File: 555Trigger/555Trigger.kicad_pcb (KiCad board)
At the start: 2 copper layers, 39 parts, among them J1 Conn_01x03_Socket, J2 Conn_01x02_Socket, J3 Strobing_LED_1, J4 Strobing_LED_2, U7 74LVC2G74, U8 74AHC2G00, U9 OPA2333xxD

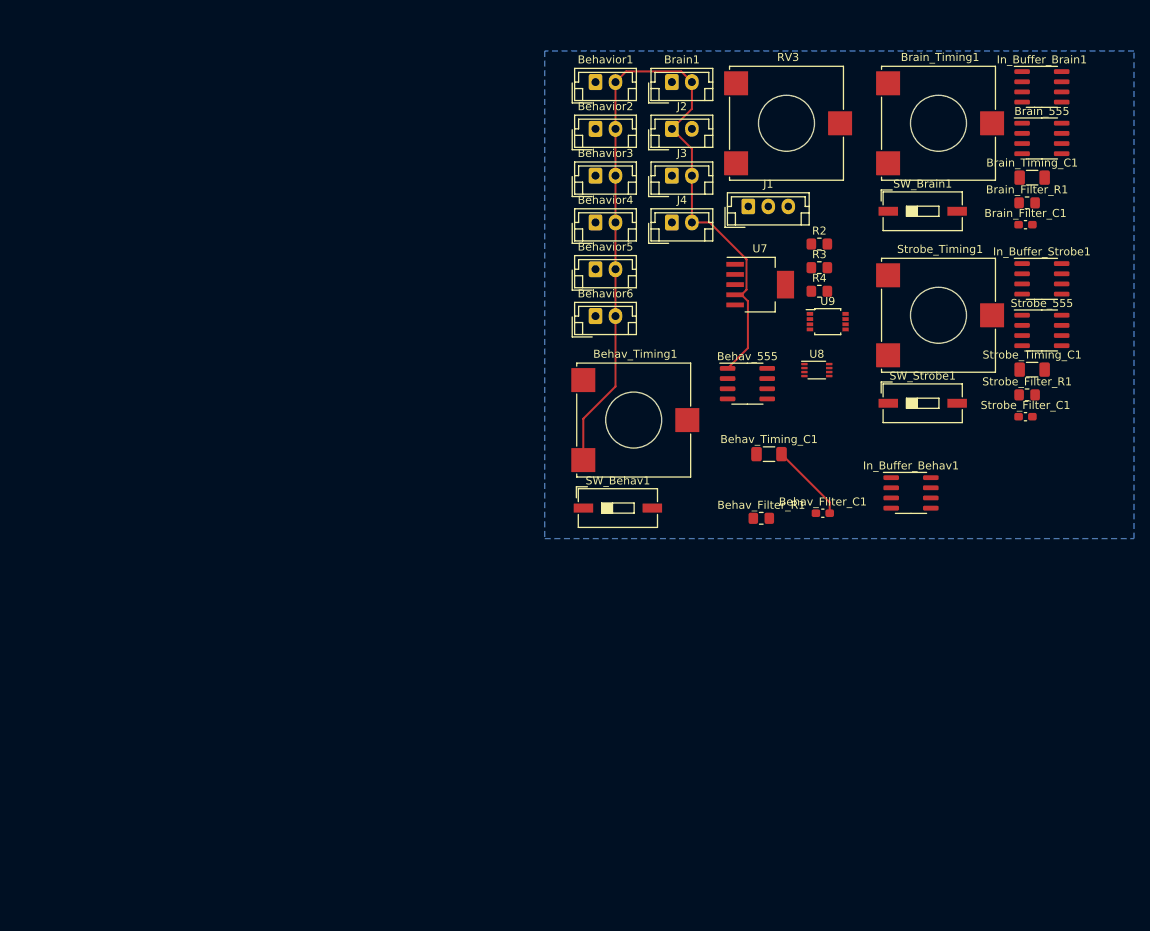
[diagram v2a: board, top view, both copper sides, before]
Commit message: updated timer design
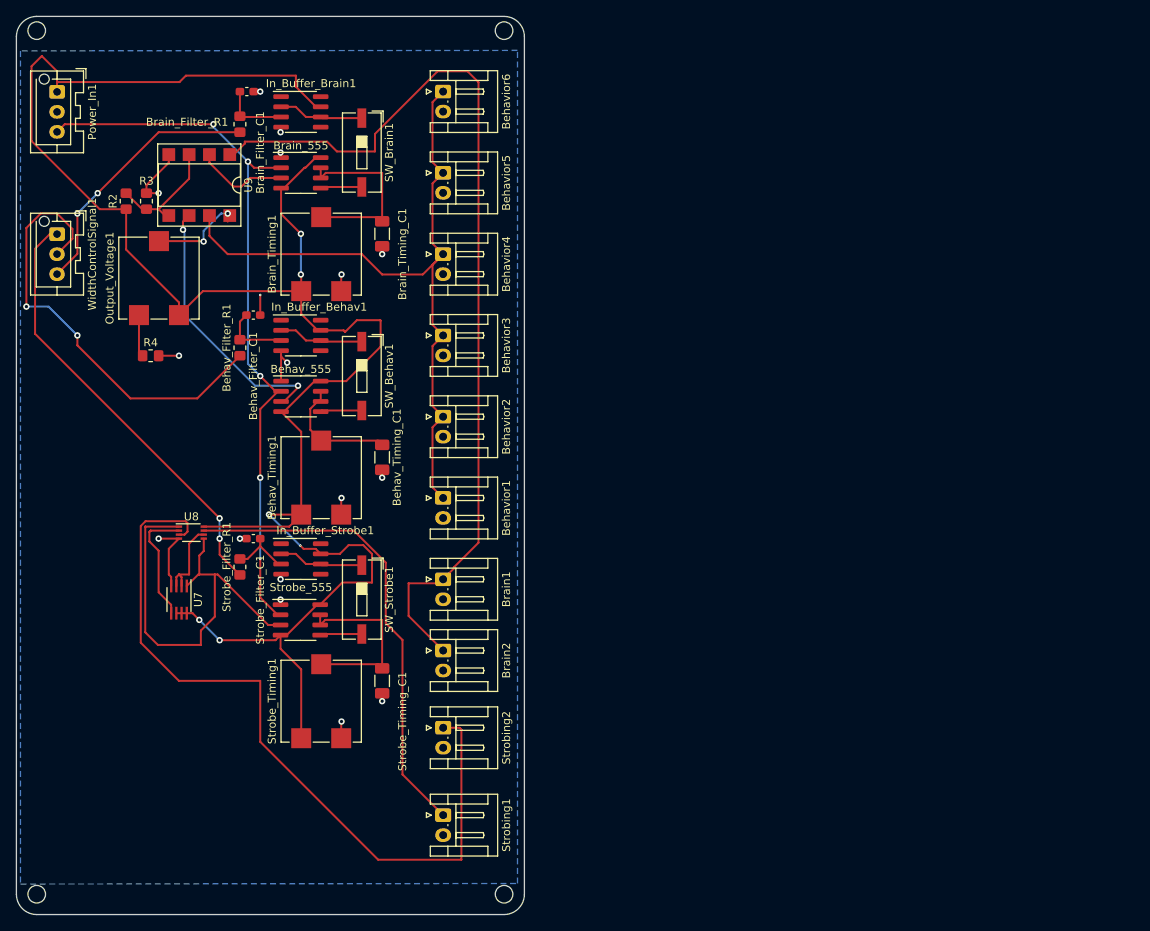
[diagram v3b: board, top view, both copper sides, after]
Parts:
- removed J2: Conn_01x02_Socket, Connector_JST:JST_EH_B2B-EH-A_1x02_P2.50mm_Vertical
- added Brain2: Conn_01x02_Socket, Connector_JST:JST_EH_S2B-EH_1x02_P2.50mm_Horizontal, F.Cu at (78.7, 100.3)
- added H1: MountingHole, MountingHole:MountingHole_2.2mm_M2, F.Cu at (86.4, 22.9)
- added H2: MountingHole, MountingHole:MountingHole_2.2mm_M2, F.Cu at (27.9, 22.9)
- added H3: MountingHole, MountingHole:MountingHole_2.2mm_M2, F.Cu at (27.9, 130.8)
- added H4: MountingHole, MountingHole:MountingHole_2.2mm_M2, F.Cu at (86.4, 130.8)
- added Power_In1: Conn_01x03_Socket, Connector_JST:JST_XA_B03B-XASK-1-A_1x03_P2.50mm_Vertical, F.Cu at (30.5, 30.5)
- Behav_555, Brain_555, Strobe_555: value ~ -> TLC555xD
- Behav_Timing1, Brain_Timing1, Strobe_Timing1: footprint Potentiometer_SMD:Potentiometer_ACP_CA14-VSMD_Vertical_Hole -> Potentiometer_SMD:Potentiometer_ACP_CA9-VSMD_Vertical
- Behavior1, Behavior2, Behavior3, Behavior4, Behavior5, Behavior6, Brain1: footprint Connector_JST:JST_EH_B2B-EH-A_1x02_P2.50mm_Vertical -> Connector_JST:JST_EH_S2B-EH_1x02_P2.50mm_Horizontal
- Output_Voltage1: renamed from RV3; footprint Potentiometer_SMD:Potentiometer_ACP_CA14-VSMD_Vertical_Hole -> Potentiometer_SMD:Potentiometer_ACP_CA9-VSMD_Vertical
- Strobing1: renamed from J3; value Strobing_LED_1 -> Conn_01x02_Socket; footprint Connector_JST:JST_EH_B2B-EH-A_1x02_P2.50mm_Vertical -> Connector_JST:JST_EH_S2B-EH_1x02_P2.50mm_Horizontal
- Strobing2: renamed from J4; value Strobing_LED_2 -> Conn_01x02_Socket; footprint Connector_JST:JST_EH_B2B-EH-A_1x02_P2.50mm_Vertical -> Connector_JST:JST_EH_S2B-EH_1x02_P2.50mm_Horizontal
- U7: footprint Package_TO_SOT_SMD:SOT-223-6_TabPin3 -> Package_SO:SSOP-8_2.95x2.8mm_P0.65mm
- U9: footprint Package_SO:OnSemi_Micro8 -> Package_DIP:DIP-8_W7.62mm_SMDSocket_SmallPads
- WidthControlSignal1: renamed from J1; footprint Connector_JST:JST_EH_B3B-EH-A_1x03_P2.50mm_Vertical -> Connector_JST:JST_XA_B03B-XASK-1-A_1x03_P2.50mm_Vertical
- moved Strobe_Filter_R1 100.7 mm to (53.3, 89.9), turned to 90 degrees
- moved Strobe_555 99.5 mm to (60.9, 96.5)
- moved In_Buffer_Strobe1 99.0 mm to (61.0, 88.9)
- moved Brain_Filter_R1 98.9 mm to (53.3, 34.6), turned to 90 degrees
- moved Brain_Filter_C1 98.7 mm to (54.2, 30.5)
- moved Strobe_Filter_C1 97.7 mm to (55.0, 86.4), turned to 180 degrees
- moved Brain_555 92.7 mm to (61.0, 40.6)
- moved In_Buffer_Brain1 92.7 mm to (61.0, 33.0)
- moved Strobe_Timing1 91.2 mm to (63.5, 106.7), turned to 90 degrees
- moved Strobe_Timing_C1 90.1 mm to (71.1, 104.1), turned to -90 degrees
- moved R2 86.8 mm to (39.1, 44.2), turned to 90 degrees
- moved WidthControlSignal1 86.5 mm to (30.5, 48.3), turned to -90 degrees
- moved Strobing1 84.9 mm to (78.7, 120.9), turned to -90 degrees
- moved R3 84.5 mm to (41.7, 44.2), turned to 90 degrees
- moved R4 84.0 mm to (42.2, 63.5)
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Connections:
- net /Behavior_Camera_Unit/Trigger_In renamed VAC
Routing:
- net +5V: track 0.00 -> 246.8 mm, vias 0 -> 6
- net Net-(Brain1-Pin_1): track 0.00 -> 117.0 mm
- net Net-(Strobing2-Pin_1): track 0.00 -> 97.5 mm
- net VAC: track 0.00 -> 92.2 mm, vias 0 -> 5
- net Net-(Behavior1-Pin_1): track 0.00 -> 91.1 mm
- net GND: track 113.9 -> 40.1 mm, vias 0 -> 17
- net Net-(Strobing1-Pin_1): track 0.00 -> 58.9 mm
- net /Behavior_Camera_Unit/CV_In: track 0.00 -> 55.5 mm, vias 0 -> 2
- net /Strobing_Trigger/CV_In: track 0.00 -> 54.9 mm, vias 0 -> 2
- net /Strobing_Trigger/Trigger_Out: track 0.00 -> 54.2 mm
- net /Behavior_Camera_Unit/Trigger_Out: track 0.00 -> 34.2 mm, vias 0 -> 2
- net /Brain_Camera_Unit/CV_In: track 0.00 -> 33.2 mm, vias 0 -> 2
- net Net-(Strobe_555-DIS): track 0.00 -> 23.2 mm
- net Net-(Brain_555-DIS): track 0.00 -> 23.1 mm
- net Net-(Behav_555-DIS): track 0.00 -> 15.3 mm
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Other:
- board outline added: 63.5 x 112.3 mm

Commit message: changed some components to make manufacturing simpler
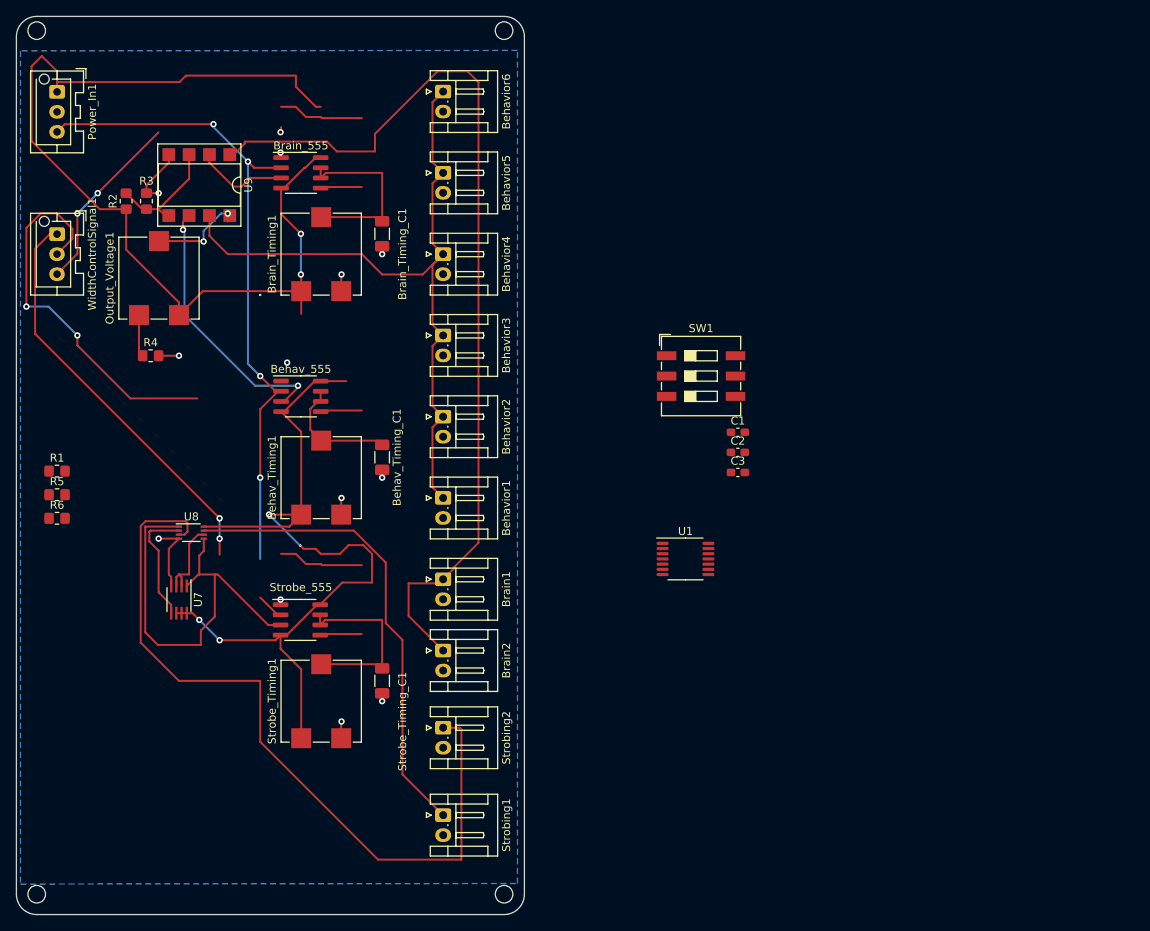
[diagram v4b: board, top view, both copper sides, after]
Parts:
- removed Behav_Filter_C1, Brain_Filter_C1, Strobe_Filter_C1: 10 pF, Capacitor_SMD:C_0603_1608Metric_Pad1.08x0.95mm_HandSolder
- removed Behav_Filter_R1, Brain_Filter_R1, Strobe_Filter_R1: 32k, Resistor_SMD:R_0805_2012Metric_Pad1.20x1.40mm_HandSolder
- removed In_Buffer_Behav1, In_Buffer_Brain1, In_Buffer_Strobe1: OPA333xxD, Package_SO:SOIC-8_3.9x4.9mm_P1.27mm
- removed SW_Behav1, SW_Brain1, SW_Strobe1: SW_DIP_x01, Button_Switch_SMD:SW_DIP_SPSTx01_Slide_9.78x4.72mm_W8.61mm_P2.54mm
- added C1: 10 nF, Capacitor_SMD:C_0603_1608Metric_Pad1.08x0.95mm_HandSolder, F.Cu at (115.6, 73.1)
- added C2: 10 nF, Capacitor_SMD:C_0603_1608Metric_Pad1.08x0.95mm_HandSolder, F.Cu at (115.6, 75.6)
- added C3: 10 nF, Capacitor_SMD:C_0603_1608Metric_Pad1.08x0.95mm_HandSolder, F.Cu at (115.6, 78.1)
- added R1: 32k, Resistor_SMD:R_0805_2012Metric_Pad1.20x1.40mm_HandSolder, F.Cu at (30.5, 77.9)
- added R5: 32k, Resistor_SMD:R_0805_2012Metric_Pad1.20x1.40mm_HandSolder, F.Cu at (30.5, 80.9)
- added R6: 32k, Resistor_SMD:R_0805_2012Metric_Pad1.20x1.40mm_HandSolder, F.Cu at (30.5, 83.8)
- added SW1: SW_DIP_x03, Button_Switch_SMD:SW_DIP_SPSTx03_Slide_9.78x9.8mm_W8.61mm_P2.54mm, F.Cu at (111.0, 66.0)
- added U1: OPA4196xPW, Package_SO:TSSOP-14_4.4x5mm_P0.65mm, F.Cu at (109.0, 88.9)
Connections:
- Behav_555 pad 5: Net-(Behav_555-CV) -> /Behavior_Camera_Unit/CV_In
- Brain_555 pad 5: Net-(Brain_555-CV) -> /Brain_Camera_Unit/CV_In
- Strobe_555 pad 5: Net-(Strobe_555-CV) -> /Strobing_Trigger/CV_In
- WidthControlSignal1 pad 1: /Strobing_Trigger/CV_In -> Net-(WidthControlSignal1-Pin_1)
- WidthControlSignal1 pad 2: /Behavior_Camera_Unit/CV_In -> Net-(WidthControlSignal1-Pin_2)
- WidthControlSignal1 pad 3: /Brain_Camera_Unit/CV_In -> Net-(WidthControlSignal1-Pin_3)
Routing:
- net Net-(WidthControlSignal1-Pin_1): track 0.00 -> 51.3 mm, vias 0 -> 2
- net /Behavior_Camera_Unit/CV_In: track 55.5 -> 5.20 mm, vias 2 -> 0
- net /Strobing_Trigger/CV_In: track 54.9 -> 5.27 mm, vias 2 -> 0
- net Net-(WidthControlSignal1-Pin_2): track 0.00 -> 48.0 mm, vias 0 -> 2
- net /Brain_Camera_Unit/CV_In: track 33.2 -> 5.20 mm, vias 2 -> 0
- net Net-(WidthControlSignal1-Pin_3): track 0.00 -> 23.0 mm, vias 0 -> 2
- net +5V: track 246.8 -> 226.0 mm
- net Net-(In_Buffer_Behav1--): track 10.7 -> 0.00 mm
- net GND: track 40.1 -> 30.4 mm, vias 17 -> 14
- net Net-(In_Buffer_Behav1-+): track 8.60 -> 0.00 mm
- net Net-(In_Buffer_Brain1-+): track 8.26 -> 0.00 mm
- net Net-(In_Buffer_Strobe1-+): track 7.67 -> 0.00 mm
- net Net-(Strobe_555-CV): track 5.27 -> 0.00 mm
- net Net-(Brain_555-CV): track 5.20 -> 0.00 mm
- net Net-(Behav_555-CV): track 5.20 -> 0.00 mm
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
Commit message: changed components to be easier to order
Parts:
- added U2: OPA2333xxD, Package_SO:TSSOP-8_3x3mm_P0.65mm, F.Cu at (45.7, 73.7)
- Behav_Timing1, Brain_Timing1, Output_Voltage1, Strobe_Timing1: footprint Potentiometer_SMD:Potentiometer_ACP_CA9-VSMD_Vertical -> Potentiometer_SMD:Potentiometer_Bourns_3314J_Vertical
- Behav_Timing_C1, Brain_Timing_C1, Strobe_Timing_C1: value 1.7u -> 2.2uF; footprint Capacitor_SMD:C_1206_3216Metric_Pad1.33x1.80mm_HandSolder -> Capacitor_SMD:C_0805_2012Metric
- C1, C2, C3: footprint Capacitor_SMD:C_0603_1608Metric_Pad1.08x0.95mm_HandSolder -> Capacitor_SMD:C_0603_1608Metric
- R1, R2, R3, R4, R5, R6: footprint Resistor_SMD:R_0805_2012Metric_Pad1.20x1.40mm_HandSolder -> Resistor_SMD:R_0402_1005Metric
- U1: value OPA4196xPW -> OPA2333xxD; footprint Package_SO:TSSOP-14_4.4x5mm_P0.65mm -> Package_SO:TSSOP-8_3x3mm_P0.65mm
- U9: footprint Package_DIP:DIP-8_W7.62mm_SMDSocket_SmallPads -> Package_SO:TSSOP-8_3x3mm_P0.65mm
- moved C3 79.7 mm to (36.4, 68.5)
- moved C1 79.7 mm to (36.4, 63.5)
- moved C2 79.7 mm to (36.4, 66.0)
- moved SW1 76.5 mm to (35.6, 78.7)
- moved U1 66.5 mm to (45.7, 68.6)
- moved R1 14.8 mm to (30.5, 63.1)
- moved R5 14.8 mm to (30.5, 66.0)
- moved R6 14.8 mm to (30.5, 69.0)
- moved Strobe_Timing1 2.00 mm to (63.5, 104.7), turned to 180 degrees
- turned Behav_Timing1 to 180 degrees
- turned Brain_Timing1 to 180 degrees
- turned Output_Voltage1 to 180 degrees
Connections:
- C3 pad 1: Net-(U1C-+) -> Net-(U2A-+)
- R6 pad 2: Net-(U1C-+) -> Net-(U2A-+)
- SW1 pad 3: Net-(U1C--) -> Net-(U2A--)
- U1 pad 4: +5V -> GND
- U1 pad 8: Net-(U1C--) -> +5V
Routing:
- net /Brain_Camera_Unit/CV_In: track 5.20 -> 51.4 mm, vias 0 -> 2
- net /Strobing_Trigger/CV_In: track 5.27 -> 38.6 mm, vias 0 -> 2
- net Net-(WidthControlSignal1-Pin_2): track 48.0 -> 17.3 mm, vias 2 -> 0
- net Net-(WidthControlSignal1-Pin_1): track 51.3 -> 24.1 mm, vias 2 -> 0
- net Net-(U1A--): track 0.00 -> 22.8 mm, vias 0 -> 2
- net /Behavior_Camera_Unit/CV_In: track 5.20 -> 27.7 mm, vias 0 -> 2
- net Net-(U1B--): track 0.00 -> 21.3 mm, vias 0 -> 2
- net Net-(U1B-+): track 0.00 -> 19.9 mm, vias 0 -> 2
- net +5V: track 226.0 -> 207.2 mm
- net Net-(U2A--): track 0.00 -> 17.1 mm
- net Net-(U2A-+): track 0.00 -> 17.1 mm, vias 0 -> 2
- net Net-(U1A-+): track 0.00 -> 15.9 mm
- net Net-(WidthControlSignal1-Pin_3): track 23.0 -> 10.7 mm, vias 2 -> 0
- net GND: track 30.4 -> 42.1 mm, vias 14 -> 18
- net Net-(In_Buffer_Brain1--): track 10.7 -> 0.00 mm
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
